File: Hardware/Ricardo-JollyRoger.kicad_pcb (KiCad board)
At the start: 4 copper layers, 45.8 x 35.8 mm, 87 parts, among them J1 RBUS, J2 USB_C_Receptacle_USB2.0, J3 Conn_01x08_Pin, U1 ESP32-S3, U2 SN65HVD230, U3 LM66200DRLR, U4 MAX77827AEFD+T, U5 SC4215ASTRT, U7 LM66200DRLR, Y1 R940000171

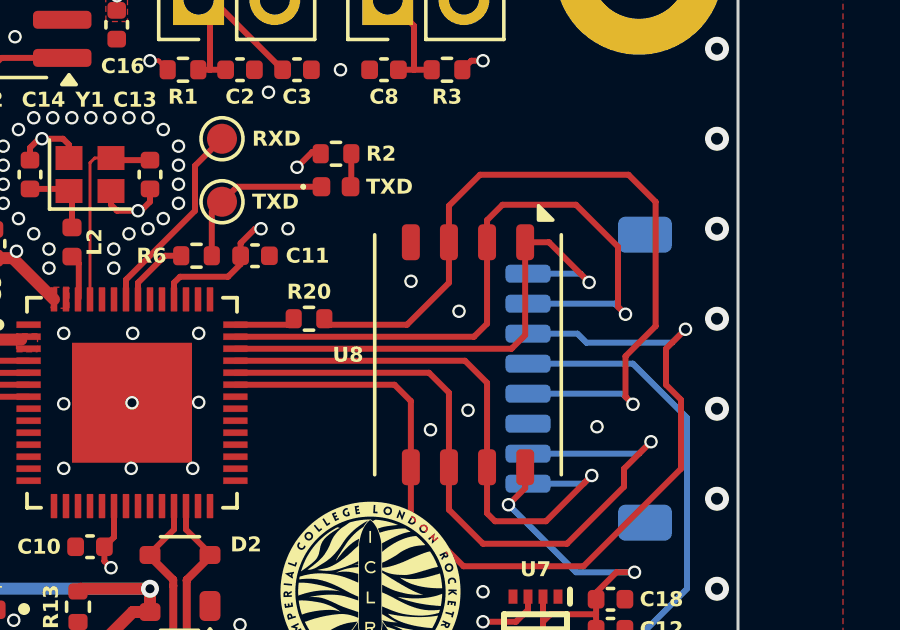
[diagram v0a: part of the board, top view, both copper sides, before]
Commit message: Added labels for NAND pinout
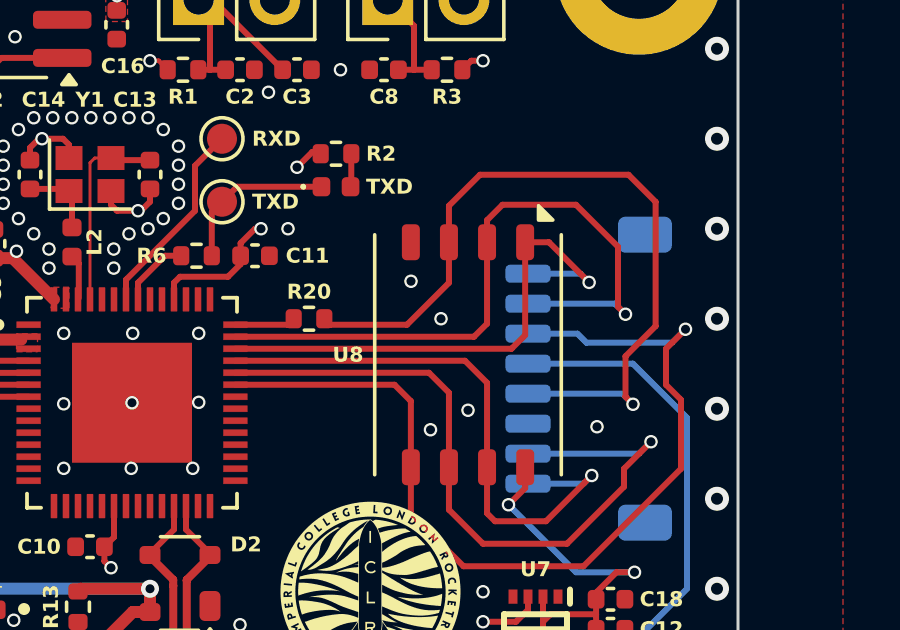
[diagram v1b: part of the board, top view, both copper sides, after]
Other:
- board text added: "CD/DAT3"
- board text added: "CLK"
- board text added: "CMD"
- board text added: "DAT0"
- board text added: "DAT1"
- board text added: "DAT2"
- board text added: "VDD"
- board text added: "VSS"
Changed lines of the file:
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@@
 		)
 	)
+	(gr_text "VSS"
+		(at 116.825 63.49 0)
+		(layer "B.SilkS")
+		(effects
+			(font
+				(size 0.5 0.5)
+				(thickness 0.1)
+				(bold yes)
+			)
+			(justify left mirror)
+		)
+	)
+	(gr_text "DAT0"
+		(at 116.825 64.49 0)
+		(layer "B.SilkS")
+		(effects
+			(font
+				(size 0.5 0.5)
+				(thickness 0.1)
+				(bold yes)
+			)
+			(justify left mirror)
+		)
+	)
+	(gr_text "CMD"
+		(at 116.825 60.49 0)
+		(layer "B.SilkS")
+		(effects
+			(font
+				(size 0.5 0.5)
+				(thickness 0.1)
+				(bold yes)
+			)
+			(justify left mirror)
+		)
+	)
+	(gr_text "DAT2"
+		(at 116.825 58.49 0)
+		(layer "B.SilkS")
+		(effects
+			(font
+				(size 0.5 0.5)
+				(thickness 0.1)
+				(bold yes)
+			)
+			(justify left mirror)
+		)
+	)
 	(gr_text "{dblquote}Not all treasure is silver and gold, mate{dblquote}"
 		(at 102.925 49.59 0)
@@
 		)
 	)
+	(gr_text "CLK"
+		(at 116.825 62.49 0)
+		(layer "B.SilkS")
+		(effects
+			(font
+				(size 0.5 0.5)
+				(thickness 0.1)
+				(bold yes)
+			)
+			(justify left mirror)
+		)
+	)
+	(gr_text "CD/DAT3"
+		(at 116.825 59.49 0)
+		(layer "B.SilkS")
+		(effects
+			(font
+				(size 0.5 0.5)
+				(thickness 0.1)
+				(bold yes)
+			)
+			(justify left mirror)
+		)
+	)
+	(gr_text "DAT1"
+		(at 116.825 65.49 0)
+		(layer "B.SilkS")
+		(effects
+			(font
+				(size 0.5 0.5)
+				(thickness 0.1)
+				(bold yes)
+			)
+			(justify left mirror)
+		)
+	)
+	(gr_text "VDD"
+		(at 116.825 61.49 0)
+		(layer "B.SilkS")
+		(effects
+			(font
+				(size 0.5 0.5)
+				(thickness 0.1)
+				(bold yes)
+			)
+			(justify left mirror)
+		)
+	)
 	(gr_text "BBOUT"
 		(at 93.425 67.49 0)
@@
 	)
 	(via
-		(at 115.625 59.74)
+		(at 115.025 59.99)
 		(size 0.45)
 		(drill 0.3)
@@
 	)
 	(zone
-		(net 3)
-		(net_name "VBUS")
-		(layer "F.Cu")
-		(name "$teardrop_padvia$")
-		(hatch full 0.1)
-		(priority 30000)
-		(attr
-			(teardrop
-				(type padvia)
-			)
-		)
-		(connect_pads yes
-			(clearance 0)
-		)
-		(min_thickness 0.0254)
-		(filled_areas_thickness no)
-		(fill yes
-			(thermal_gap 0.5)
-			(thermal_bridge_width 0.5)
-			(island_removal_mode 1)
-			(island_area_min 10)
-		)
-		(polygon
-			(pts
-				(xy 87.241888 72.023468) (xy 87.641888 72.023468) (xy 87.732873 71.676104) (xy 87.525 71.589) (xy 87.3 71.59)
-			)
-		)
-	)
-	(zone
 		(net 0)
 		(net_name "")
@@
 	)
 	(zone
-		(net 1)
-		(net_name "GND")
-		(layer "F.Cu")
-		(name "$teardrop_padvia$")
-		(hatch full 0.1)
-		(priority 30002)
-		(attr
-			(teardrop
-				(type padvia)
-			)
-		)
-		(connect_pads yes
-			(clearance 0)
-		)
-		(min_thickness 0.0254)
-		(filled_areas_thickness no)
-		(fill yes
-			(thermal_gap 0.5)
-			(thermal_bridge_width 0.5)
-			(island_removal_mode 1)
-			(island_area_min 10)
-		)
-		(polygon
-			(pts
-				(xy 88.316888 72.386882) (xy 88.566888 72.386882) (xy 88.649761 72.022986) (xy 88.441888 71.935882)
-				(xy 88.234015 72.022986)
-			)
-		)
-	)
-	(zone
 		(net 2)
 		(net_name "+3V3")
@@
 	)
 	(zone
+		(net 3)
+		(net_name "VBUS")
+		(layer "F.Cu")
+		(name "$teardrop_padvia$")
+		(hatch full 0.1)
+		(priority 30000)
+		(attr
+			(teardrop
+				(type padvia)
+			)
+		)
+		(connect_pads yes
+			(clearance 0)
+		)
+		(min_thickness 0.0254)
+		(filled_areas_thickness no)
+		(fill yes
+			(thermal_gap 0.5)
+			(thermal_bridge_width 0.5)
+			(island_removal_mode 1)
+			(island_area_min 10)
+		)
+		(polygon
+			(pts
+				(xy 87.241888 72.023468) (xy 87.641888 72.023468) (xy 87.732873 71.676104) (xy 87.525 71.589) (xy 87.3 71.59)
+			)
+		)
+	)
+	(zone
 		(net 76)
 		(net_name "Net-(C6-Pad1)")
@@
 	)
 	(zone
-		(net 8)
-		(net_name "/Power/LX1")
+		(net 1)
+		(net_name "GND")
 		(layer "F.Cu")
-		(hatch edge 0.508)
-		(priority 5)
+		(name "$teardrop_padvia$")
+		(hatch full 0.1)
+		(priority 30002)
+		(attr
+			(teardrop
+				(type padvia)
+			)
+		)
 		(connect_pads yes
 			(clearance 0)
 		)
-		(min_thickness 0.254)
+		(min_thickness 0.0254)
 		(filled_areas_thickness no)
 		(fill yes
-			(thermal_gap 0.508)
-			(thermal_bridge_width 0.508)
-			(smoothing fillet)
-			(radius 0.1)
+			(thermal_gap 0.5)
+			(thermal_bridge_width 0.5)
+			(island_removal_mode 1)
+			(island_area_min 10)
 		)
 		(polygon
 			(pts
-				(xy 92.313167 74.02865) (xy 92.122888 74.326882) (xy 92.124419 74.641518) (xy 92.124885 74.641518)
-				(xy 92.126352 75.042916) (xy 90.947911 75.043916) (xy 90.947885 74.641518) (xy 91.765629 74.641518)
-				(xy 91.764888 74.365882) (xy 91.875888 74.125882) (xy 91.872888 73.853882) (xy 91.872749 73.821137)
-				(xy 92.303596 73.819625)
+				(xy 88.316888 72.386882) (xy 88.566888 72.386882) (xy 88.649761 72.022986) (xy 88.441888 71.935882)
+				(xy 88.234015 72.022986)
 			)
 		)
 	)
 	(zone
-		(net 2)
-		(net_name "+3V3")
+		(net 8)
+		(net_name "/Power/LX1")
 		(layer "F.Cu")
 		(hatch edge 0.508)
-		(priority 4)
+		(priority 5)
 		(connect_pads yes
-			(clearance 0.2)
+			(clearance 0)
 		)
 		(min_thickness 0.254)
@@
 			(thermal_bridge_width 0.508)
 			(smoothing fillet)
+			(radius 0.1)
 		)
 		(polygon
 			(pts
-				(xy 94.825 60.34) (xy 94.825 58.74) (xy 96.375 58.74) (xy 96.375 60.34)
+				(xy 92.313167 74.02865) (xy 92.122888 74.326882) (xy 92.124419 74.641518) (xy 92.124885 74.641518)
+				(xy 92.126352 75.042916) (xy 90.947911 75.043916) (xy 90.947885 74.641518) (xy 91.765629 74.641518)
+				(xy 91.764888 74.365882) (xy 91.875888 74.125882) (xy 91.872888 73.853882) (xy 91.872749 73.821137)
+				(xy 92.303596 73.819625)
 			)
 		)
@@
 	)
 	(zone
+		(net 2)
+		(net_name "+3V3")
+		(layer "F.Cu")
+		(hatch edge 0.508)
+		(priority 4)
+		(connect_pads yes
+			(clearance 0.2)
+		)
+		(min_thickness 0.254)
+		(filled_areas_thickness no)
+		(fill yes
+			(thermal_gap 0.508)
+			(thermal_bridge_width 0.508)
+			(smoothing fillet)
+		)
+		(polygon
+			(pts
+				(xy 94.825 60.34) (xy 94.825 58.74) (xy 96.375 58.74) (xy 96.375 60.34)
+			)
+		)
+	)
+	(zone
 		(net 0)
 		(net_name "")
@@
 		(name "$teardrop_padvia$")
 		(hatch full 0.1)
-		(priority 30002)
+		(priority 30000)
 		(attr
 			(teardrop
@@
 		(polygon
 			(pts
-				(xy 87.730112 75.442263) (xy 87.447269 75.725106) (xy 87.747789 76.060981) (xy 87.907595 75.902589)
-				(xy 88.065987 75.742783)
+				(xy 87.325 72.04) (xy 87.725 72.04) (xy 87.75 71.59) (xy 87.525 71.589) (xy 87.3 71.59)
+			)
+		)
+	)
+	(zone
+		(net 3)
+		(net_name "VBUS")
+		(layer "B.Cu")
+		(name "$teardrop_padvia$")
+		(hatch full 0.1)
+		(priority 30001)
+		(attr
+			(teardrop
+				(type padvia)
+			)
+		)
+		(connect_pads yes
+			(clearance 0)
+		)
+		(min_thickness 0.0254)
+		(filled_areas_thickness no)
+		(fill yes
+			(thermal_gap 0.5)
+			(thermal_bridge_width 0.5)
+			(island_removal_mode 1)
+			(island_area_min 10)
+		)
+		(polygon
+			(pts
+				(xy 87.984619 71.413224) (xy 87.701776 71.130381) (xy 87.365901 71.430901) (xy 87.524293 71.590707)
+				(xy 87.684099 71.749099)
 			)
 		)
@@
 	)
 	(zone
-		(net 3)
-		(net_name "VBUS")
-		(layer "B.Cu")
-		(name "$teardrop_padvia$")
-		(hatch full 0.1)
-		(priority 30000)
-		(attr
-			(teardrop
-				(type padvia)
-			)
-		)
-		(connect_pads yes
-			(clearance 0)
-		)
-		(min_thickness 0.0254)
-		(filled_areas_thickness no)
-		(fill yes
-			(thermal_gap 0.5)
-			(thermal_bridge_width 0.5)
-			(island_removal_mode 1)
-			(island_area_min 10)
-		)
-		(polygon
-			(pts
-				(xy 87.325 72.04) (xy 87.725 72.04) (xy 87.75 71.59) (xy 87.525 71.589) (xy 87.3 71.59)
-			)
-		)
-	)
-	(zone
 		(net 1)
 		(net_name "GND")
@@
 		(name "$teardrop_padvia$")
 		(hatch full 0.1)
-		(priority 30001)
+		(priority 30002)
 		(attr
 			(teardrop
@@
 		(polygon
 			(pts
-				(xy 87.984619 71.413224) (xy 87.701776 71.130381) (xy 87.365901 71.430901) (xy 87.524293 71.590707)
-				(xy 87.684099 71.749099)
+				(xy 87.730112 75.442263) (xy 87.447269 75.725106) (xy 87.747789 76.060981) (xy 87.907595 75.902589)
+				(xy 88.065987 75.742783)
 			)
 		)

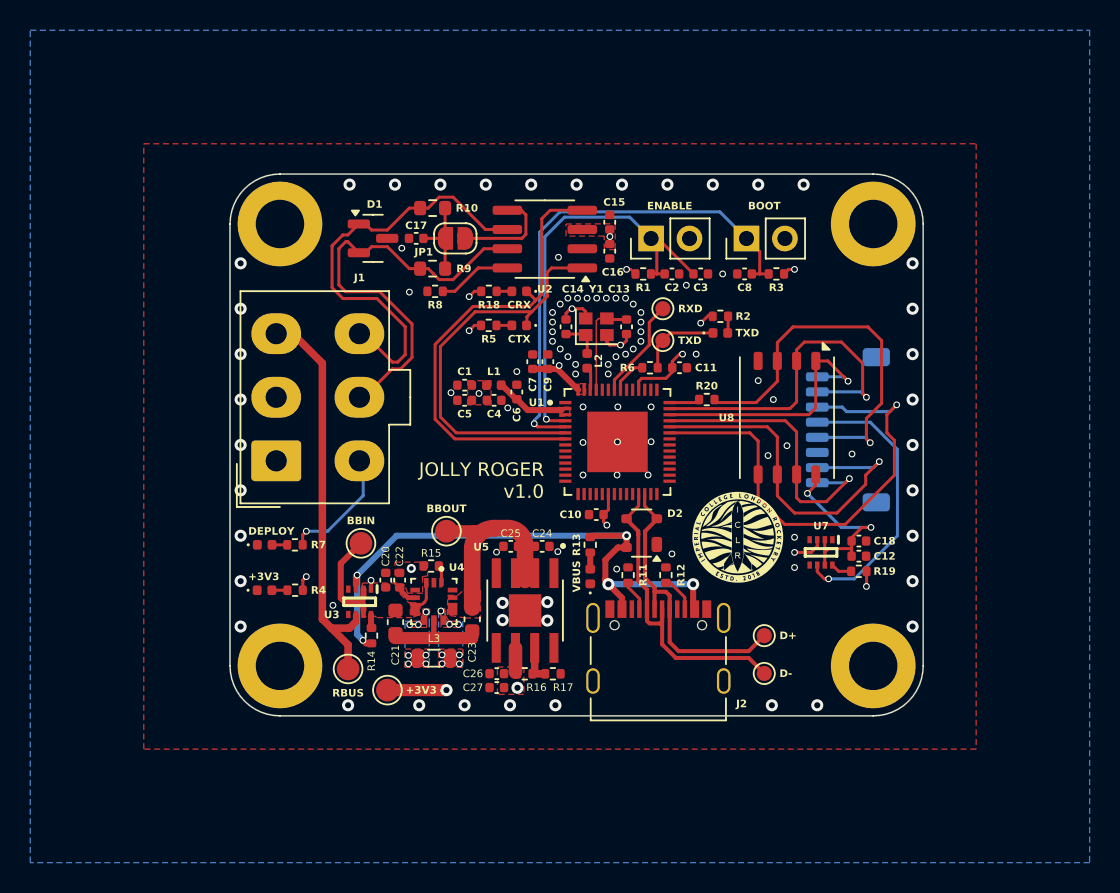
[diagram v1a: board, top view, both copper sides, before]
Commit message: Reduce edge via size
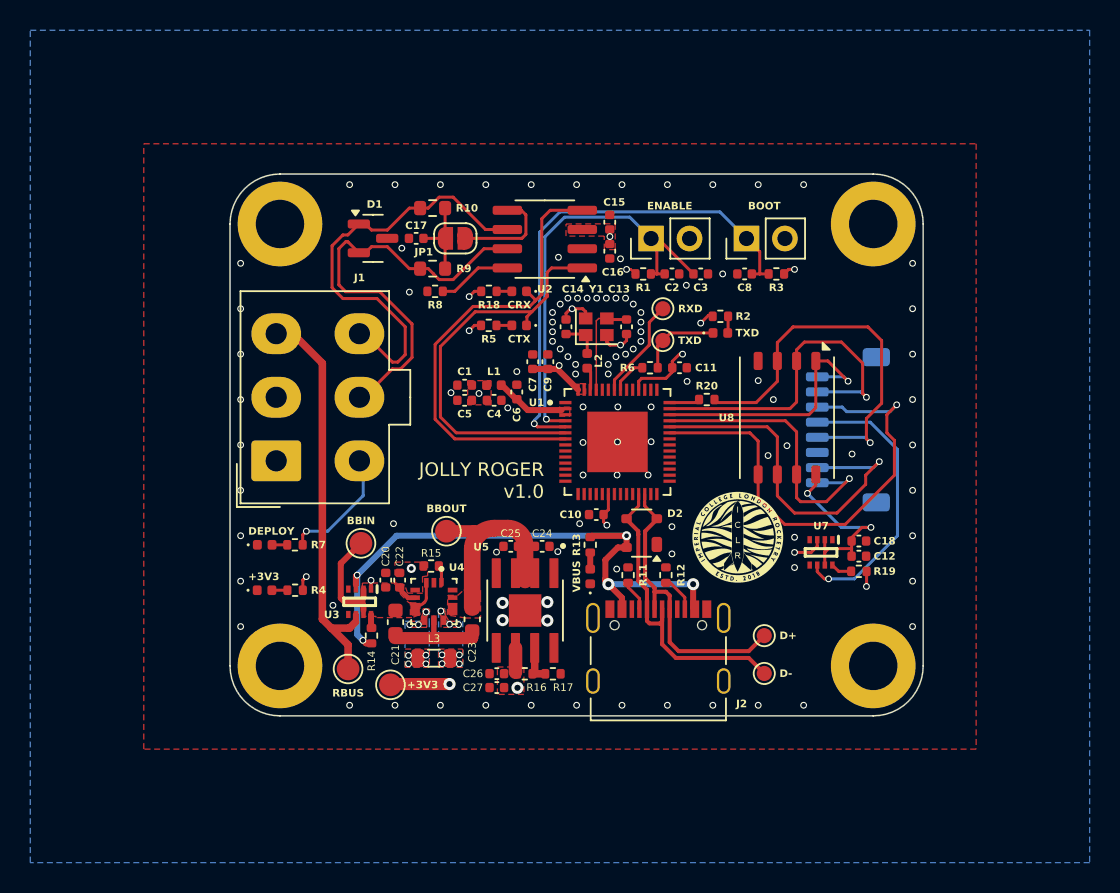
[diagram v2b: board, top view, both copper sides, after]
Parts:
- moved TP6 0.40 mm to (89.7, 78.8)
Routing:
- net GND: vias 100 -> 108

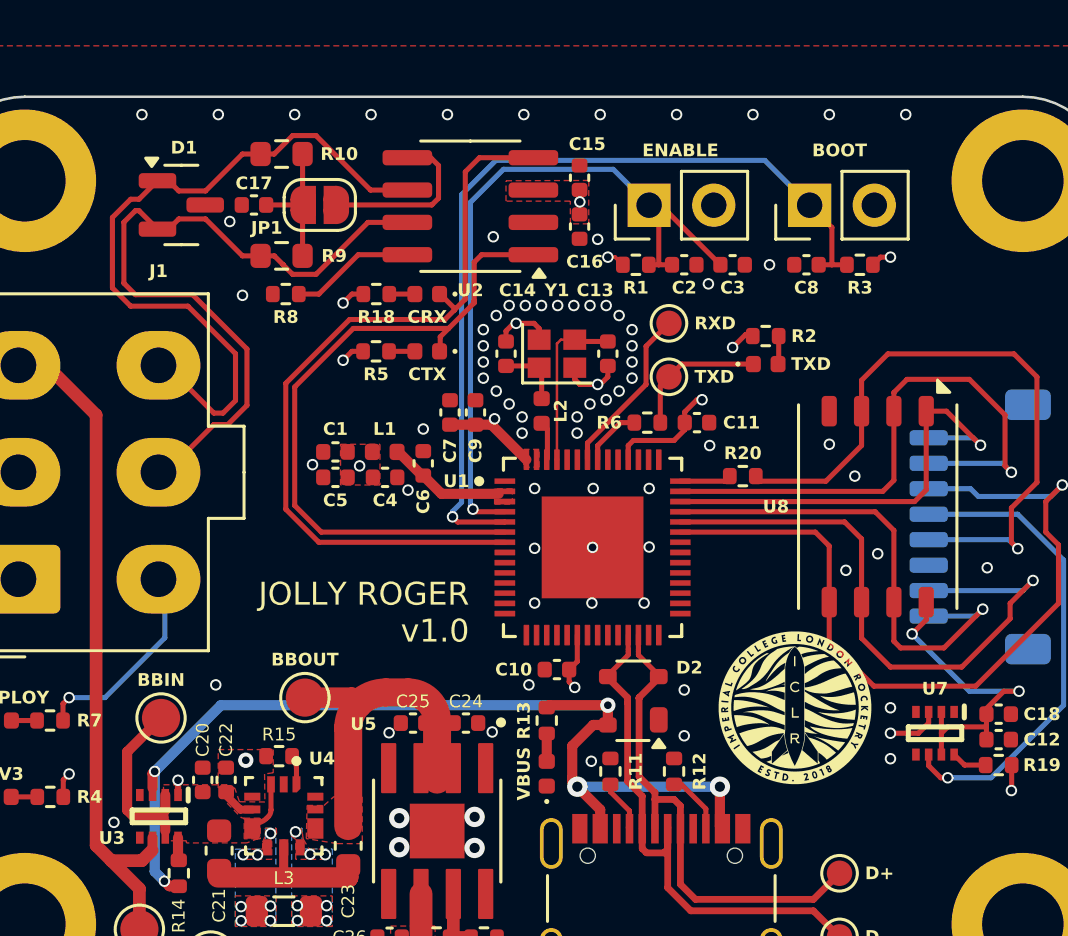
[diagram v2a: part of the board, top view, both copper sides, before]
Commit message: Added GPIO breakout
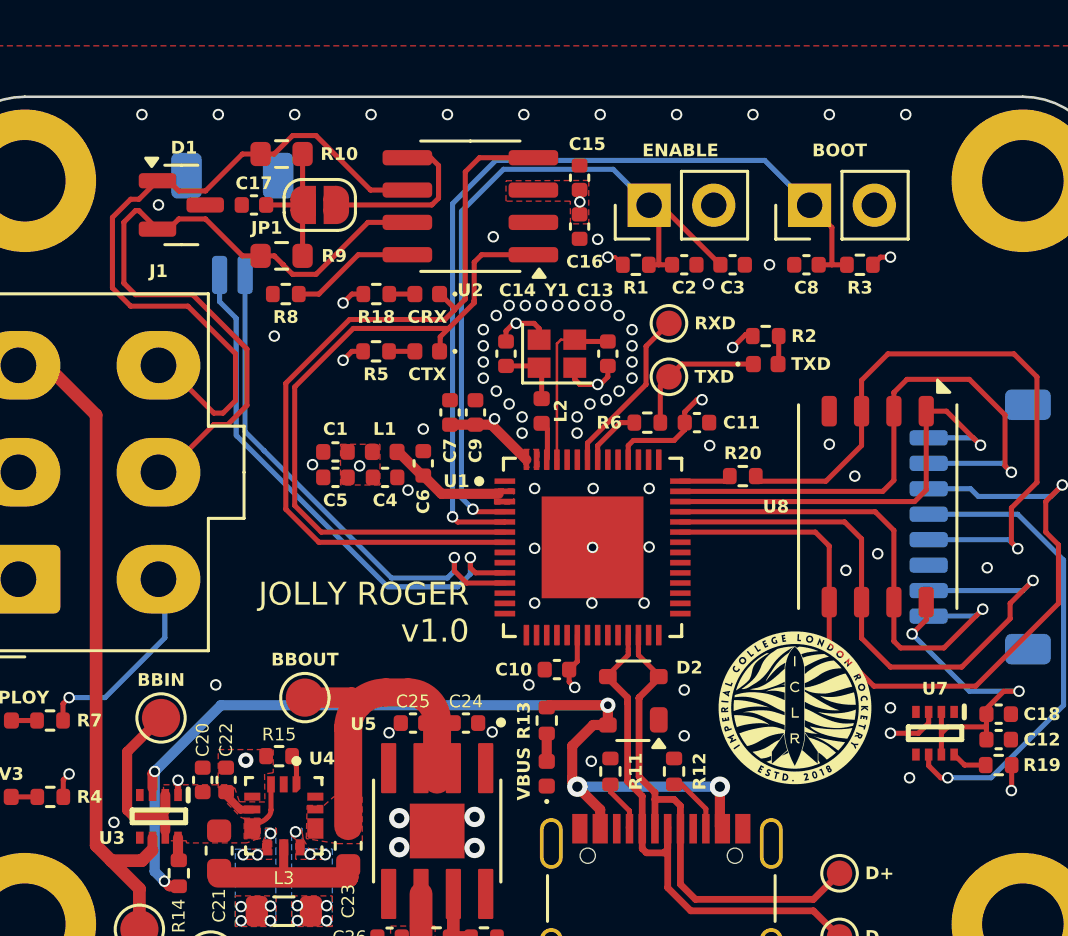
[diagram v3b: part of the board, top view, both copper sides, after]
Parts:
- added J4: Conn_01x02_Pin, Connector_Molex:Molex_Pico-Clasp_202396-0207_1x02-1MP_P1.00mm_Horizontal, B.Cu at (90.6, 50.1)
- H3: moved to B.Cu
- moved REF** 0.64 mm to (103.1, 63.2)
- turned H3 to 180 degrees
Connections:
- U1 pad 10: unconnected-(U1-GPIO5/ADC1_CH4-Pad10) -> /GPIO5
- U1 pad 11: unconnected-(U1-GPIO6/ADC1_CH5-Pad11) -> /GPIO6
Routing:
- net /GPIO5: track 0.00 -> 20.9 mm, vias 0 -> 1
- net /GPIO6: track 0.00 -> 20.1 mm, vias 0 -> 1
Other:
- board text added: "GPIO5"
- board text added: "GPIO6"

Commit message: Rearranged NAND
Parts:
- moved U8 4.16 mm to (120.1, 61.2)
- moved C12 2.55 mm to (120.5, 67.8)
- moved C18 2.55 mm to (120.5, 66.8)
- moved R19 2.55 mm to (120.5, 68.8)
- moved U7 2.55 mm to (118.0, 67.5)
- moved G*** 0.80 mm to (112.7, 68.3)
- moved TP10 0.30 mm to (108.0, 54.0)
- moved TP9 0.30 mm to (108.0, 56.1)
- moved J3 0.27 mm to (119.7, 62.0)
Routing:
- net /NAND_CMD: track 31.6 -> 17.2 mm
- net /NAND_CLK: track 26.0 -> 15.8 mm
- net /HEADER_3V3: track 18.9 -> 11.8 mm
- net /NAND_SD2: track 17.8 -> 23.7 mm
- net /NAND_SD0: track 24.5 -> 18.8 mm
- net /NAND_3V3: track 13.0 -> 8.00 mm, vias 2 -> 0
- net /NAND_SD1: track 19.5 -> 22.5 mm
- net /NAND_SD3: track 22.9 -> 20.5 mm
